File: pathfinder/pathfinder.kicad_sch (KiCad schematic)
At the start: 17 parts, among them J3 CAS left, J4 CAS right, U1 STM32F042C6Ux

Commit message: Start components layout
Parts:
- C3, C4, C5, C6, C7: footprint Capacitor_SMD:C_0603_1608Metric_Pad1.08x0.95mm_HandSolder -> Capacitor_SMD:C_0402_1005Metric_Pad0.74x0.62mm_HandSolder
- D1, D2: footprint Diode_SMD:D_0603_1608Metric_Pad1.05x0.95mm_HandSolder -> Diode_SMD:D_0402_1005Metric_Pad0.77x0.64mm_HandSolder
- R3, R4: footprint Resistor_SMD:R_0603_1608Metric_Pad0.98x0.95mm_HandSolder -> Resistor_SMD:R_0402_1005Metric_Pad0.72x0.64mm_HandSolder
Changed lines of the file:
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@@
 			)
 		)
-		(property "Footprint" "Capacitor_SMD:C_0603_1608Metric_Pad1.08x0.95mm_HandSolder"
+		(property "Footprint" "Capacitor_SMD:C_0402_1005Metric_Pad0.74x0.62mm_HandSolder"
 			(at 97.79 44.45 0)
 			(effects
@@
 			)
 		)
-		(property "Footprint" "Resistor_SMD:R_0603_1608Metric_Pad0.98x0.95mm_HandSolder"
+		(property "Footprint" "Resistor_SMD:R_0402_1005Metric_Pad0.72x0.64mm_HandSolder"
 			(at 34.29 167.64 0)
 			(effects
@@
 			)
 		)
-		(property "Footprint" "Capacitor_SMD:C_0603_1608Metric_Pad1.08x0.95mm_HandSolder"
+		(property "Footprint" "Capacitor_SMD:C_0402_1005Metric_Pad0.74x0.62mm_HandSolder"
 			(at 77.47 44.45 0)
 			(effects
@@
 			)
 		)
-		(property "Footprint" "Resistor_SMD:R_0603_1608Metric_Pad0.98x0.95mm_HandSolder"
+		(property "Footprint" "Resistor_SMD:R_0402_1005Metric_Pad0.72x0.64mm_HandSolder"
 			(at 34.29 152.4 0)
 			(effects
@@
 			)
 		)
-		(property "Footprint" "Capacitor_SMD:C_0603_1608Metric_Pad1.08x0.95mm_HandSolder"
+		(property "Footprint" "Capacitor_SMD:C_0402_1005Metric_Pad0.74x0.62mm_HandSolder"
 			(at 118.11 44.45 0)
 			(effects
@@
 			)
 		)
-		(property "Footprint" "Capacitor_SMD:C_0603_1608Metric_Pad1.08x0.95mm_HandSolder"
+		(property "Footprint" "Capacitor_SMD:C_0402_1005Metric_Pad0.74x0.62mm_HandSolder"
 			(at 107.95 44.45 0)
 			(effects
@@
 			)
 		)
-		(property "Footprint" "Capacitor_SMD:C_0603_1608Metric_Pad1.08x0.95mm_HandSolder"
+		(property "Footprint" "Capacitor_SMD:C_0402_1005Metric_Pad0.74x0.62mm_HandSolder"
 			(at 87.63 44.45 0)
 			(effects
@@
 			)
 		)
-		(property "Footprint" "Diode_SMD:D_0603_1608Metric_Pad1.05x0.95mm_HandSolder"
+		(property "Footprint" "Diode_SMD:D_0402_1005Metric_Pad0.77x0.64mm_HandSolder"
 			(at 24.13 152.4 90)
 			(effects
@@
 			)
 		)
-		(property "Footprint" "Diode_SMD:D_0603_1608Metric_Pad1.05x0.95mm_HandSolder"
+		(property "Footprint" "Diode_SMD:D_0402_1005Metric_Pad0.77x0.64mm_HandSolder"
 			(at 24.13 167.64 90)
 			(effects
@@
 		)
 		(instances
-			(project "sensor_fuser"
+			(project "pathfinder"
 				(path "/07668456-3e33-43d1-9c6d-92adc10437c4"
 					(page "4")
@@
 		)
 		(instances
-			(project "sensor_fuser"
+			(project "pathfinder"
 				(path "/07668456-3e33-43d1-9c6d-92adc10437c4"
 					(page "5")
@@
 		)
 		(instances
-			(project "sensor_fuser"
+			(project "pathfinder"
 				(path "/07668456-3e33-43d1-9c6d-92adc10437c4"
 					(page "2")
@@
 		)
 		(instances
-			(project "sensor_fuser"
+			(project "pathfinder"
 				(path "/07668456-3e33-43d1-9c6d-92adc10437c4"
 					(page "7")
@@
 		)
 		(instances
-			(project "sensor_fuser"
+			(project "pathfinder"
 				(path "/07668456-3e33-43d1-9c6d-92adc10437c4"
 					(page "3")
@@
 		)
 		(instances
-			(project "sensor_fuser"
+			(project "pathfinder"
 				(path "/07668456-3e33-43d1-9c6d-92adc10437c4"
 					(page "6")

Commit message: Board finished
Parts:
- removed U1: STM32F042C6Ux, Package_DFN_QFN:QFN-48-1EP_7x7mm_P0.5mm_EP5.6x5.6mm, symbol MCU_ST_STM32F0:STM32F042C6Ux
- added C29, C30: 100n, Capacitor_SMD:C_0402_1005Metric_Pad0.74x0.62mm_HandSolder, symbol Device:C_Small
- added C31, C32: 23p, Capacitor_SMD:C_0402_1005Metric_Pad0.74x0.62mm_HandSolder, symbol Device:C_Small
- added D6: SZNUP2105L, Package_TO_SOT_SMD:SOT-23, symbol Power_Protection:SZNUP2105L
- added IC6: TCAN3413DDFR, pathfinder:SOT65P280X110-8N, symbol pathfinder:TCAN3413DDFR
- added JP1: CAN jumper, Jumper:SolderJumper-2_P1.3mm_Open_RoundedPad1.0x1.5mm, symbol Jumper:Jumper_2_Small_Open
- added R11: 3.3k, Resistor_SMD:R_0402_1005Metric_Pad0.72x0.64mm_HandSolder, symbol Device:R_Small
- added R5: 420, Resistor_SMD:R_0402_1005Metric_Pad0.72x0.64mm_HandSolder, symbol Device:R_Small
- added R6: 120, Resistor_SMD:R_0402_1005Metric_Pad0.72x0.64mm_HandSolder, symbol Device:R_Small
- added U1: STM32G431CBUx, Package_DFN_QFN:QFN-48-1EP_7x7mm_P0.5mm_EP5.6x5.6mm, symbol MCU_ST_STM32G4:STM32G431CBUx
- added Y1: 16Mhz, Crystal:Crystal_SMD_2016-4Pin_2.0x1.6mm, symbol Device:Crystal_GND24
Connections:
- net +3V3: now also J3.3 (Pin_3), C29.1, C30.1, IC6.3 (VCC), IC6.5 (VIO), R5.2; no longer J4.10 (Pin_10)
- net DEBUG_LED0: now also U1.32 (PA10)
- net DEBUG_LED1: now also U1.31 (PA9)
- net GND: now also J3.4 (Pin_4), J4.7 (Pin_7), C29.2, C30.2, C31.1, C32.1, D6.3 (A), IC6.2 (GND), U1.49 (VSS), Y1.1, Y1.3; no longer H4.1, J3.10 (Pin_10)
- net MCU_PWR: now also R11.1, U1.1 (VBAT), U1.21 (VDDA), U1.23 (VDD), U1.35 (VDD), U1.48 (VDD)
- net I2C1_SCL: now reaches J4.3 (Pin_3)
- net I2C1_SCL: now also U1.38 (PA15)
- net I2C1_SDA: now reaches J4.4 (Pin_4)
- net I2C1_SDA: now also U1.45 (PB7)
- net USART1_RX: now reaches J4.5 (Pin_5)
- net USART1_RX: now also U1.24 (PB11)
- net USART1_TX: now reaches J4.6 (Pin_6)
- net USART1_TX: now also U1.22 (PB10)
- net NRST: now reaches J4.8 (Pin_8)
- net CLK: now reaches J4.9 (Pin_9)
- net CLK: now also U1.37 (PA14)
- net SPI1_MOSI: now reaches J3.5 (Pin_5)
- net SPI1_MOSI: now also U1.15 (PA7)
- net SPI1_MISO: now reaches J3.6 (Pin_6)
- net SPI1_MISO: now also U1.14 (PA6)
- net SPI1_SCK: now reaches J3.7 (Pin_7)
- net SPI1_SCK: now also U1.13 (PA5)
- net SPI1_CS: now reaches J3.8 (Pin_8)
- net SPI1_CS: now also U1.12 (PA4)
- net CAN-: now reaches J3.9 (Pin_9)
- net CAN-: now also D6.1 (K), IC6.6 (CANL), R6.1
- new net: JP1.2 (B), R6.2
- new net: C31.2, U1.5 (PF0), Y1.4
- new net: C32.2, U1.6 (PF1), Y1.2
- new net: R5.1, U1.7 (PG10)
- new net ACC2_INT1: U1.30 (PA8)
- new net ACC2_INT2: U1.29 (PC6)
- new net BAR_INT1: U1.44 (PB6)
- new net CAN+: D6.2 (K), IC6.7 (CANH), J3.10 (Pin_10), JP1.1 (A)
- new net FDCAN_RX: IC6.4 (RXD), U1.46 (PB8)
- new net FDCAN_TX: IC6.1 (TXD), U1.47 (PB9)
- new net IMU_INT1: U1.2 (PC13)
- new net IMU_INT2: U1.3 (PC14)
- new net MAG_INT1: U1.39 (PC10)
- new net STB: IC6.8 (STB)
- new net SWD: J4.10 (Pin_10), U1.36 (PA13)
- new net SWO: U1.41 (PB3)
- new net UART1_RX: U1.11 (PA3)
- new net UART1_TX: U1.10 (PA2)
- new net USB_DM: U1.33 (PA11)
- new net USB_DP: R11.2, U1.34 (PA12)
- no-connect marks 0 -> 2
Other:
- note added: "CAN"
- moved on the sheet: C3, C4, C5, C6, C7, L1

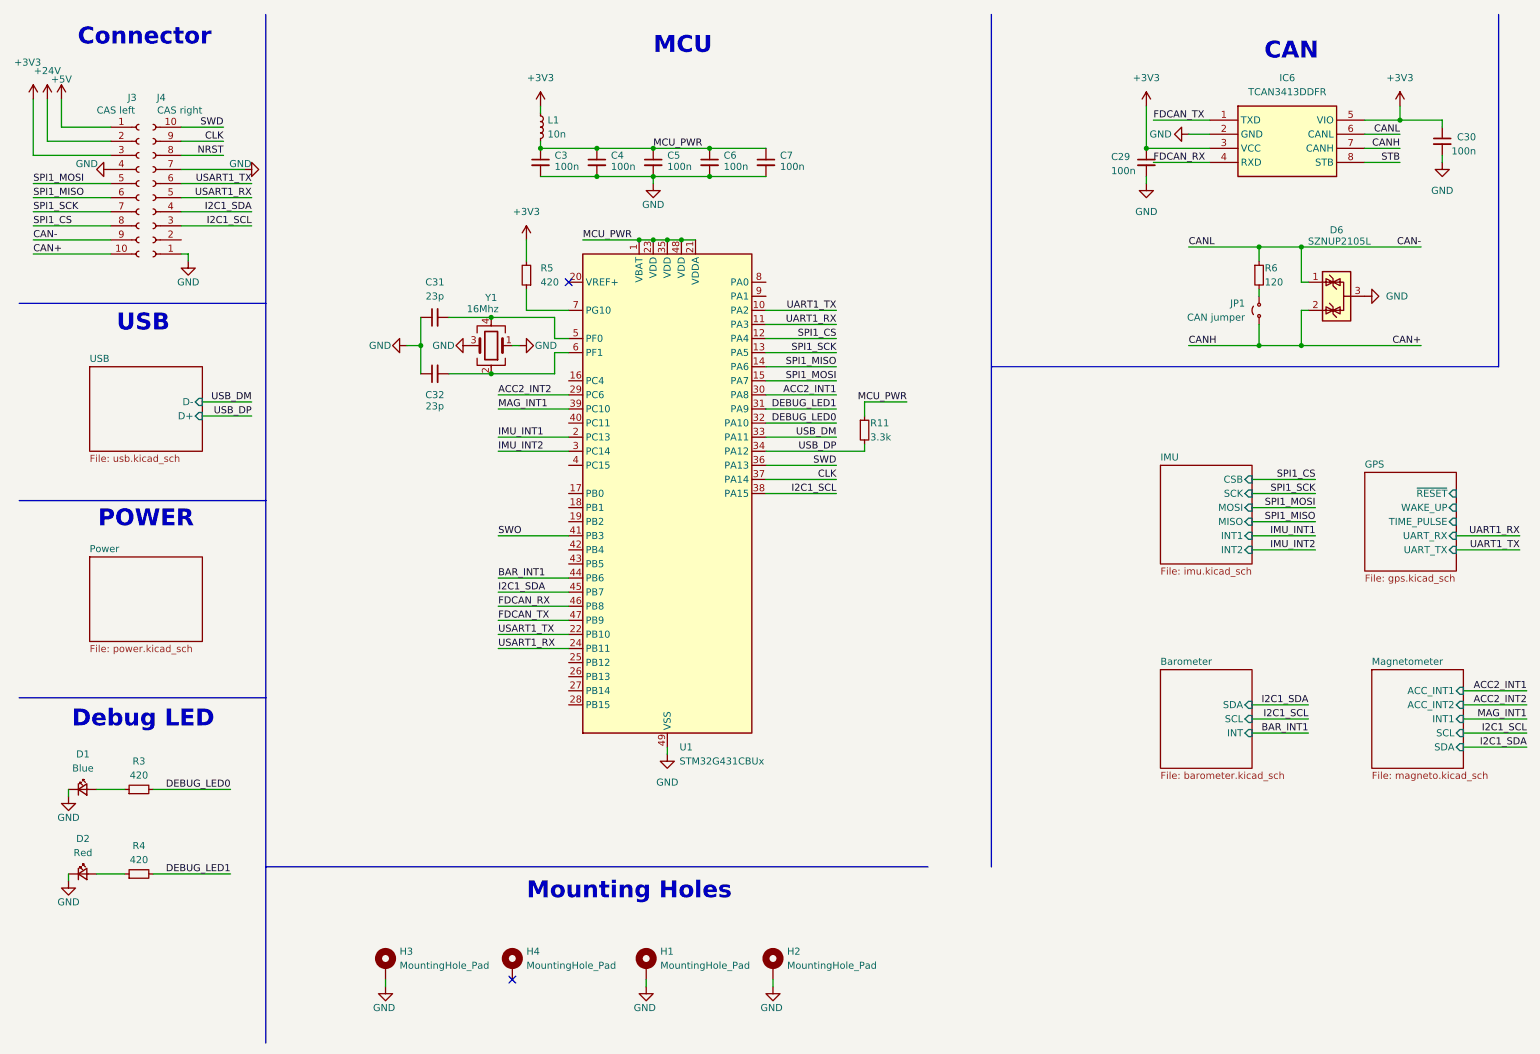
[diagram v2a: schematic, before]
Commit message: Add optocoupler
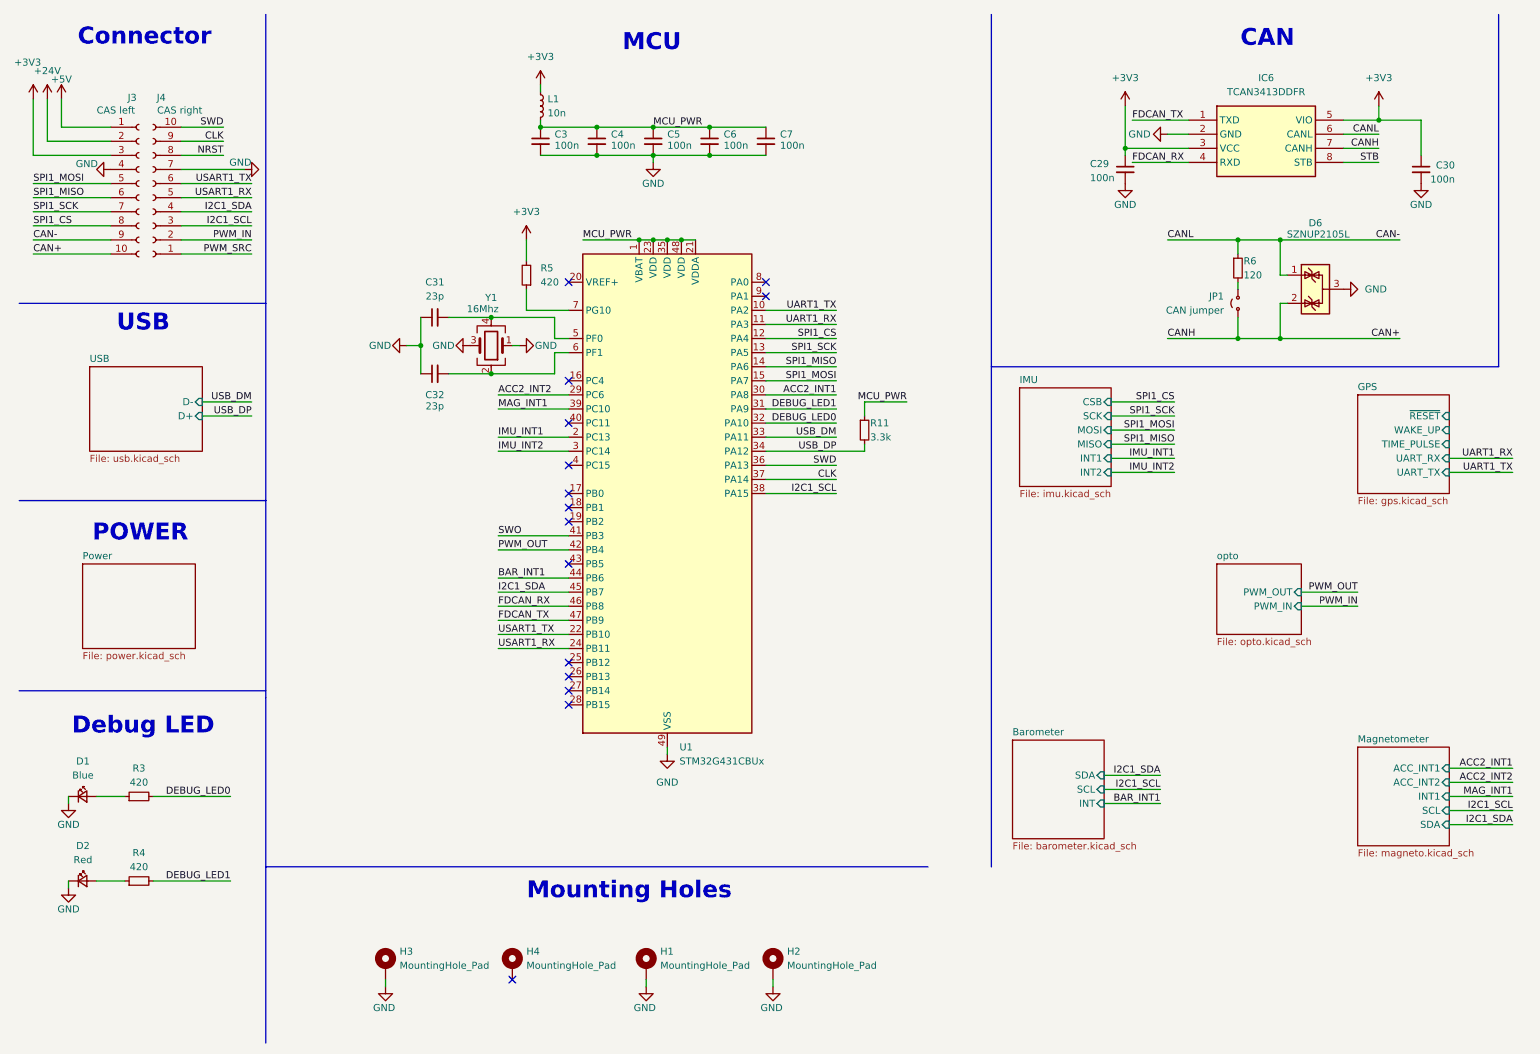
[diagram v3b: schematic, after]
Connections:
- net GND: no longer J4.1 (Pin_1)
- net PWM_IN: now reaches J4.2 (Pin_2)
- net PWM_OUT: now reaches U1.42 (PB4)
- new net PWM_SRC: J4.1 (Pin_1)
- no-connect marks 2 -> 15
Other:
- added sheet opto (opto.kicad_sch)
- moved on the sheet: C29, C3, C30, C4, C5, C6, C7, D1, D2, D6, IC6, JP1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

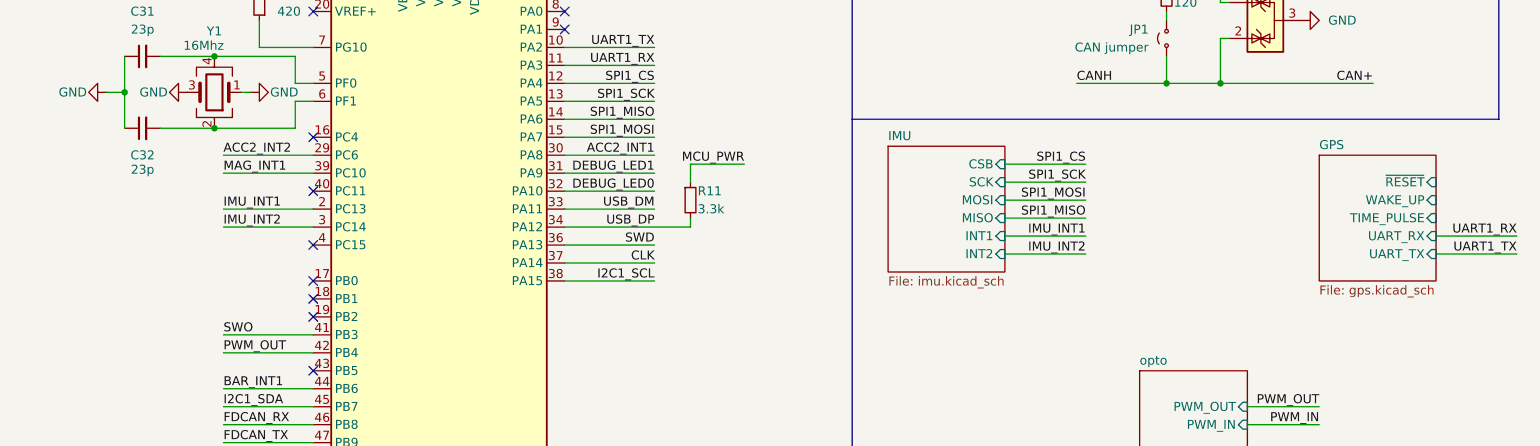
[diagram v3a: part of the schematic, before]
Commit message: change 1v8 ldo power supply
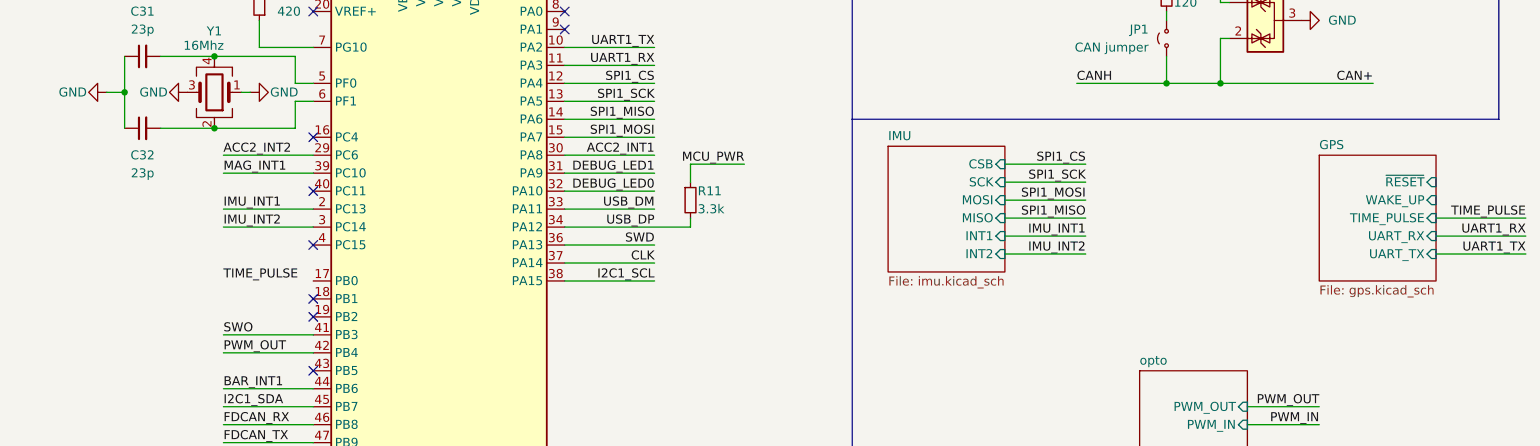
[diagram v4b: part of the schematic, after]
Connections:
- no-connect marks 15 -> 14
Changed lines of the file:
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@@
 	)
 	(no_connect
-		(at 111.76 99.06)
-	)
-	(no_connect
 		(at 111.76 60.96)
 	)
@@
 	(wire
 		(pts
+			(xy 270.51 90.17) (xy 283.21 90.17)
+		)
+		(stroke
+			(width 0)
+			(type default)
+		)
+	)
+	(wire
+		(pts
 			(xy 147.32 78.74) (xy 160.02 78.74)
 		)
@@
 	(wire
 		(pts
-			(xy 270.51 92.71) (xy 281.94 92.71)
+			(xy 270.51 92.71) (xy 283.21 92.71)
 		)
 		(stroke
@@
 	(wire
 		(pts
-			(xy 281.94 95.25) (xy 270.51 95.25)
-		)
-		(stroke
-			(width 0)
-			(type default)
-		)
-	)
-	(wire
-		(pts
 			(xy 85.09 72.39) (xy 85.09 77.47)
 		)
@@
 	(wire
 		(pts
+			(xy 270.51 95.25) (xy 283.21 95.25)
+		)
+		(stroke
+			(width 0)
+			(type default)
+		)
+	)
+	(wire
+		(pts
 			(xy 232.41 53.34) (xy 240.03 53.34)
 		)
@@
 		)
 	)
+	(label "TIME_PULSE"
+		(at 99.06 99.06 0)
+		(fields_autoplaced yes)
+		(effects
+			(font
+				(size 1.27 1.27)
+			)
+			(justify left bottom)
+		)
+	)
 	(label "CAN+"
 		(at 15.24 55.88 0)
@@
 	)
 	(label "UART1_TX"
-		(at 281.94 95.25 180)
+		(at 283.21 95.25 180)
 		(fields_autoplaced yes)
 		(effects
@@
 		)
 	)
+	(label "TIME_PULSE"
+		(at 283.21 90.17 180)
+		(fields_autoplaced yes)
+		(effects
+			(font
+				(size 1.27 1.27)
+			)
+			(justify right bottom)
+		)
+	)
 	(label "CLK"
 		(at 49.53 35.56 180)
@@
 	)
 	(label "UART1_RX"
-		(at 281.94 92.71 180)
+		(at 283.21 92.71 180)
 		(fields_autoplaced yes)
 		(effects
@@
 		(on_board yes)
 		(dnp no)
+		(fields_autoplaced yes)
 		(property "Reference" "C32"
 			(at 87.6363 81.28 90)
@@
 		)
 		(property "Value" "23p"
-			(at 87.63 83.312 90)
+			(at 87.6363 83.82 90)
 			(effects
 				(font
